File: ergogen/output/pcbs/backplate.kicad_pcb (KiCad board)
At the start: 2 copper layers, 130.3 x 107.9 mm, 5 parts

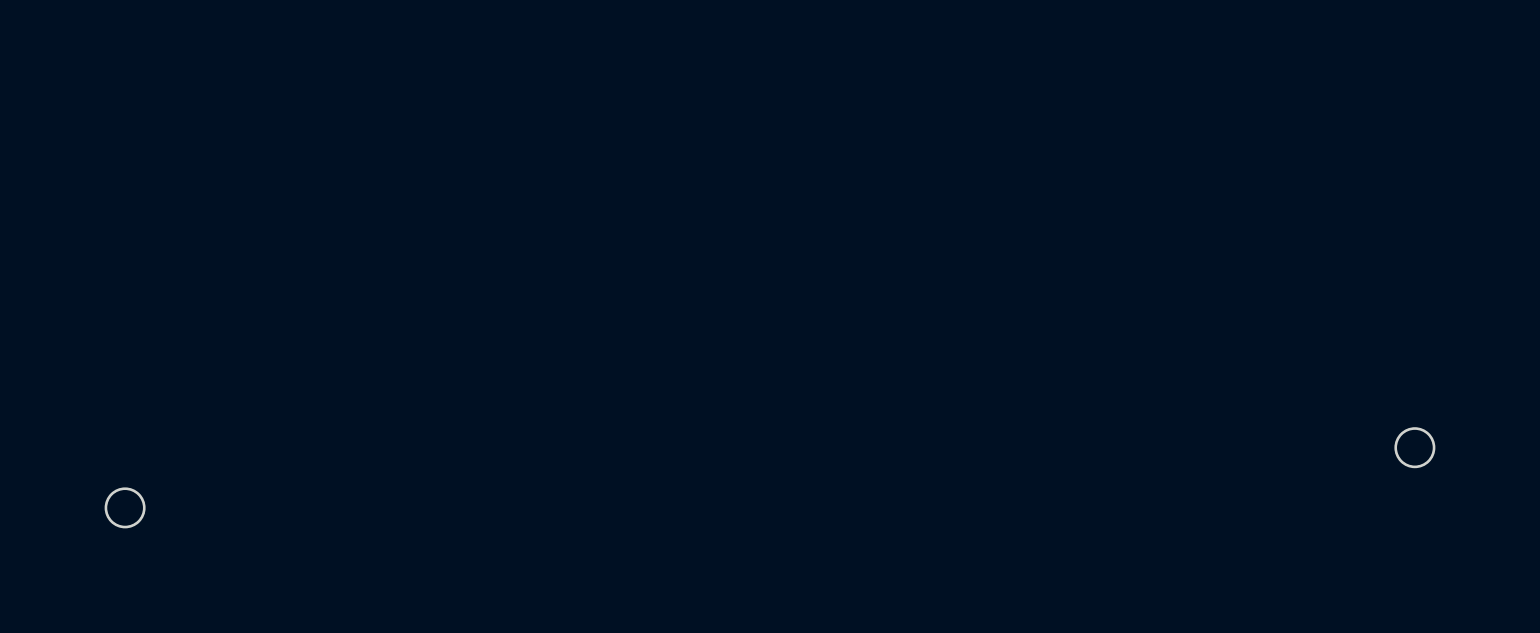
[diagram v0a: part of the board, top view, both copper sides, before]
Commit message: feat: reversible pg1316s switch footprint
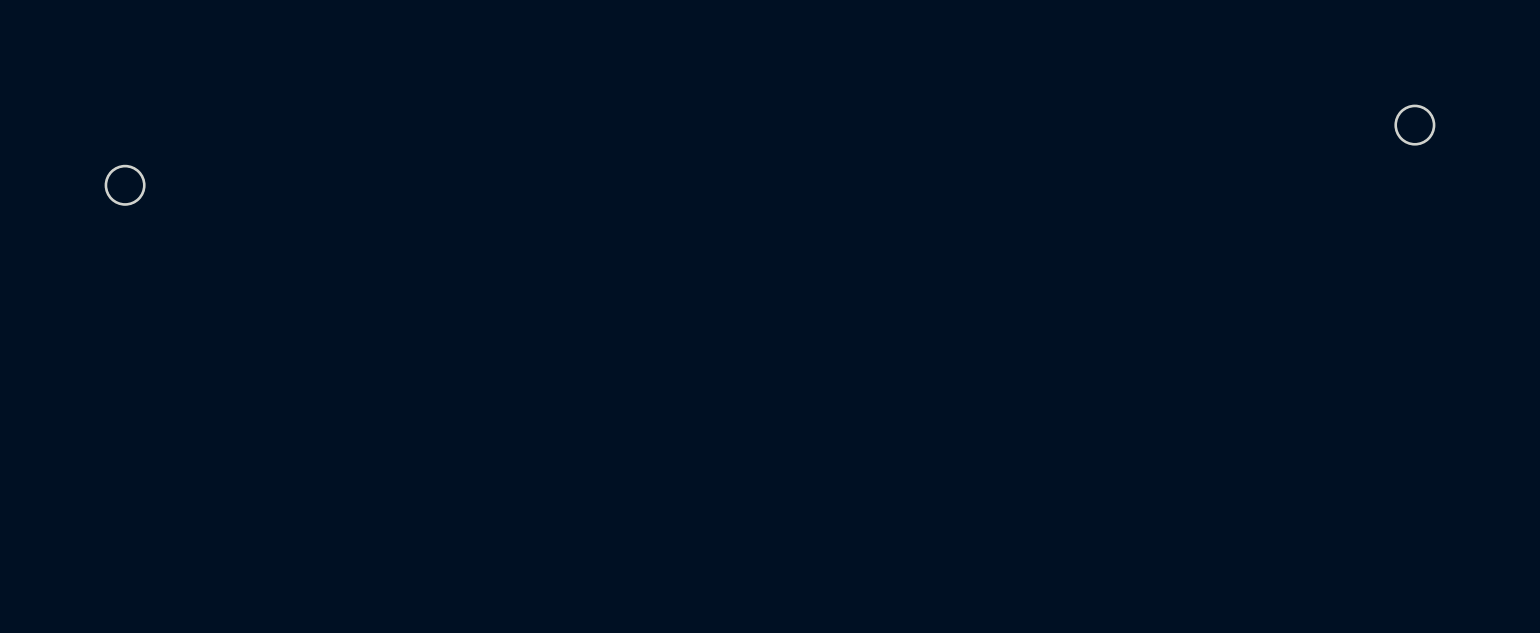
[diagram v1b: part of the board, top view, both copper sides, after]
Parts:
- moved MH1 18.5 mm to (109.2, 53.8)
- moved MH3 18.5 mm to (183.2, 50.3)
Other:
- outline, holes or cut-outs redrawn
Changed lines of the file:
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@@
   (title_block
     (title "backplate")
-    (date "2025-03-01")
+    (date "2025-03-02")
     (rev "0.2")
     (company "ceoloide")
@@
   (footprint "ceoloide:mounting_hole_npth"
     (layer "F.Cu")
-    (at 109.25 72.25 0)
+    (at 109.25 53.75 0)
     (property "Reference" "MH1"
       (at 0 2.55 0)
@@
   (footprint "ceoloide:mounting_hole_npth"
     (layer "F.Cu")
-    (at 183.218 68.7985 0)
+    (at 183.218 50.298500000000004 0)
     (property "Reference" "MH3"
       (at 0 2.55 0)
@@
 (gr_arc (start 145.75722675324377 109.20164075082414) (mid 145.57961185324376 109.04964965082414) (end 145.35231675324377 108.99501175082413) (layer Edge.Cuts) (stroke (width 0.15) (type default)))
 (gr_arc (start 91.31698635159206 108.49749067528336) (mid 91.46344595159206 108.85104337528337) (end 91.81700935159206 108.99747697528336) (layer Edge.Cuts) (stroke (width 0.15) (type default)))
-(gr_circle (center 109.25 72.25) (end 110.35 72.25) (layer Edge.Cuts) (stroke (width 0.15) (type default)) (fill none))
+(gr_circle (center 109.25 53.75) (end 110.35 53.75) (layer Edge.Cuts) (stroke (width 0.15) (type default)) (fill none))
 (gr_circle (center 109.25 90.75) (end 110.35 90.75) (layer Edge.Cuts) (stroke (width 0.15) (type default)) (fill none))
-(gr_circle (center 183.218 68.7985) (end 184.31799999999998 68.7985) (layer Edge.Cuts) (stroke (width 0.15) (type default)) (fill none))
+(gr_circle (center 183.218 50.298500000000004) (end 184.31799999999998 50.298500000000004) (layer Edge.Cuts) (stroke (width 0.15) (type default)) (fill none))
 (gr_circle (center 151.157 107.615) (end 152.257 107.615) (layer Edge.Cuts) (stroke (width 0.15) (type default)) (fill none))
 (gr_circle (center 196.7245951 115.0067481) (end 197.82459509999998 115.0067481) (layer Edge.Cuts) (stroke (width 0.15) (type default)) (fill none))
